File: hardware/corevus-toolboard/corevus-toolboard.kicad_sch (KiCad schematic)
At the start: 80 parts, among them J1 MF3, J10 1x3P, J2 XH, J3 MF3, J4 XH, J5 XH, J6 XH, J7 XH, J8 pinheader, J9 XH, Q2 NMOS, Q3 AO3401A, Q4 AO3400, Q5 AO3400, SW3 RST, U1 LIS2DE12, U2 TPS54302, U3 STM32G431KBU3, U4 TMC2209-LA, U5 MCP1416, U6 SPX3819M5-L-3-3, Y1 XRCGB25

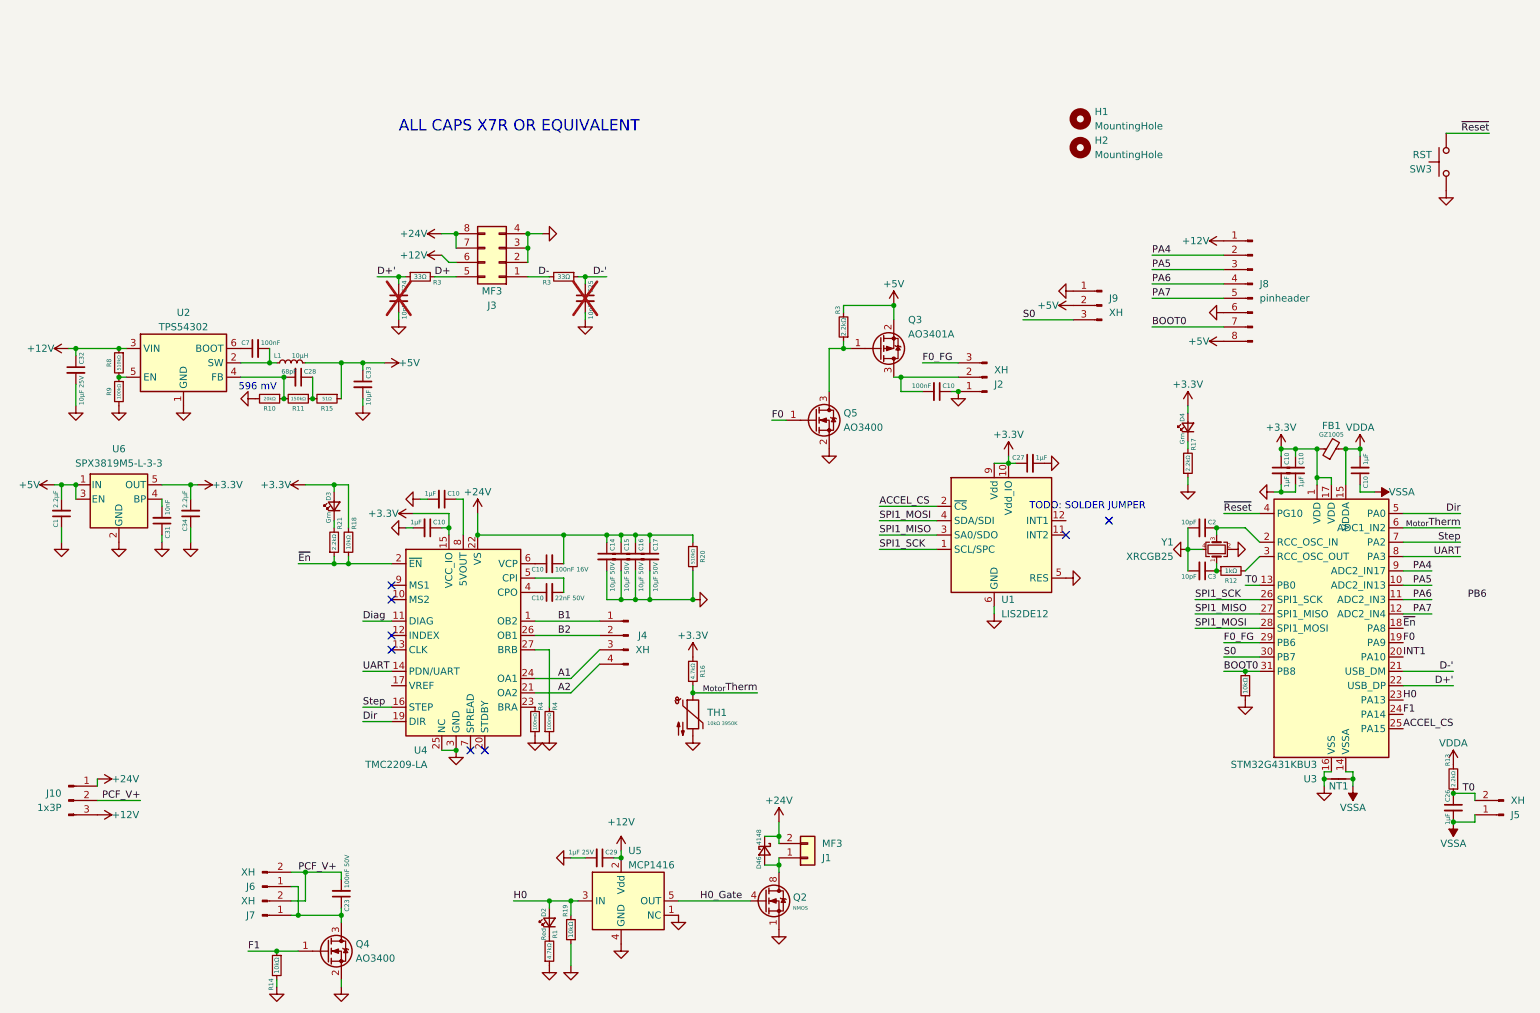
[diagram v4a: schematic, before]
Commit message: added ctb v0.3 and dual 2160, fixed typo in v0.6 manual
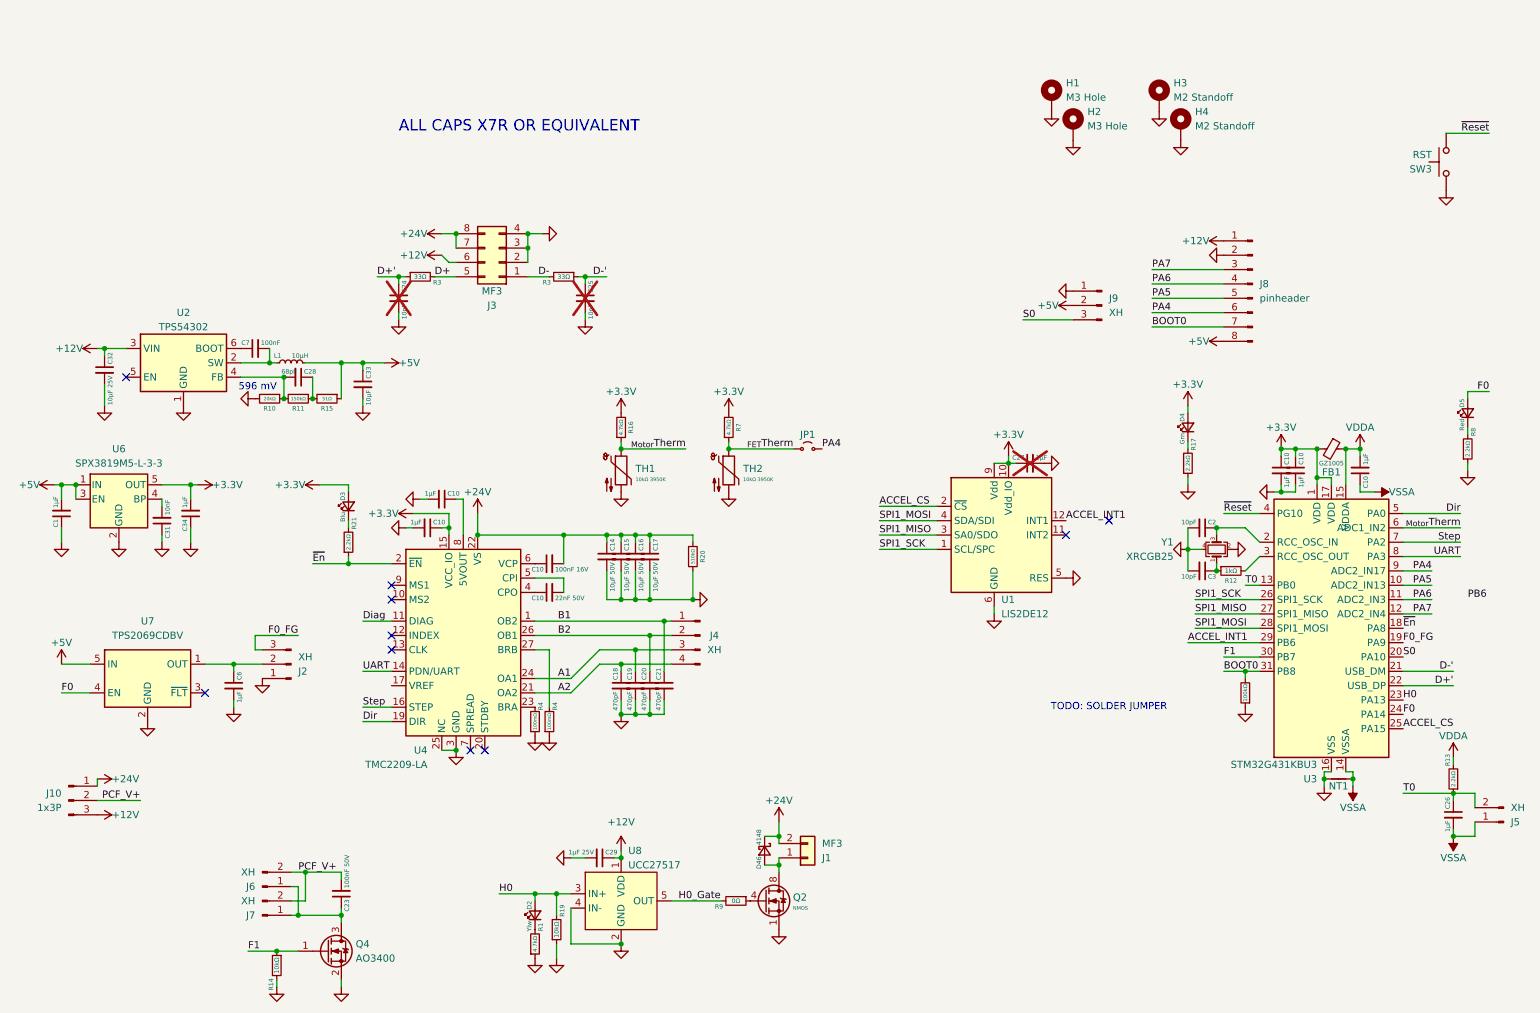
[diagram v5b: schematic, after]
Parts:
- removed C10: 100nF, AlphaLib:0402C, symbol Device:C_Small
- removed Q3: AO3401A, Package_TO_SOT_SMD:SOT-23, symbol Transistor_FET:AO3401A
- removed Q5: AO3400, Package_TO_SOT_SMD:SOT-23, symbol Device:Q_NMOS_GSD
- removed R18: 10kΩ, AlphaLib:0402R, symbol Device:R_Small
- removed R3: 2.2kΩ, AlphaLib:0402R, symbol Device:R_Small
- removed U5: MCP1416, Package_TO_SOT_SMD:SOT-23-5, symbol Driver_FET:MCP1416
- added C18, C19, C20, C21: 470pF, AlphaLib:0402C, symbol Device:C_Small
- added C6: 1µF, AlphaLib:0402C, symbol Device:C_Small
- added D5: Red, PCM_ME_passives:0603LED, symbol Device:LED_Small
- added H3, H4: M2 Standoff, corevus:Sinhoo_TH162010, symbol Mechanical:MountingHole_Pad
- added JP1: Jumper_2_Small_Open, Jumper:SolderJumper-2_P1.3mm_Open_RoundedPad1.0x1.5mm, symbol Jumper:Jumper_2_Small_Open
- added R7: 4.7kΩ, AlphaLib:0402R, symbol Device:R_Small
- added TH2: 10kΩ 3950K, AlphaLib:0402R, symbol Device:Thermistor_NTC
- added U7: TPS2069CDBV, Package_TO_SOT_SMD:SOT-23-5, symbol Power_Management:TPS2069CDBV
- added U8: UCC27517, Package_TO_SOT_SMD:SOT-23-5, symbol corevus:UCC27517
- C1, C34: value 2.2µF -> 1µF
- C27: now not fitted; now left out of the parts list
- D2: value Red -> Ylw; footprint corevus:XL1606 -> PCM_ME_passives:0603LED
- D3: value Grn -> Blu; footprint corevus:XL1606 -> PCM_ME_passives:0603LED
- D4: footprint AlphaLib:0402LED -> PCM_ME_passives:0603LED
- H1, H2: value MountingHole -> M3 Hole; footprint MountingHole:MountingHole_3.2mm_M3 -> corevus:MountingHole_M3_Driver_Corner; symbol Mechanical:MountingHole -> Mechanical:MountingHole_Pad; now left out of the parts list
- R3: value 10kΩ -> 100kΩ
- R8: value 510kΩ -> 2.2kΩ
- R9: value 100kΩ -> 0Ω
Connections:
- net INT1 is gone; now on net S0: U3.20 (PA10)
- net +12V: now also U8.1 (VDD); no longer R8.1
- net +3.3V: now also FB1.2, R7.2; no longer FB1.1
- net +5V: now also U7.5 (IN)
- net A1: now also C19.1
- net A2: now also C18.1
- net B1: now also C21.1
- net B2: now also C20.1
- net F0: now also U3.24 (PA14), D5.2 (A), U7.4 (EN); no longer U3.19 (PA9)
- net F0_FG: now also U3.19 (PA9); no longer U3.29 (PB6)
- net F1: now also U3.30 (PB7); no longer U3.24 (PA14)
- net GND: now also H1.1, H2.1, J8.2 (Pin_2), R8.1, C18.2, C19.2, C20.2, C21.2, C6.2, H3.1, H4.1, TH2.2, U7.2 (GND), U8.2 (GND), U8.4 (IN-); no longer J8.6 (Pin_6), R9.2
- net H0: now also U8.3 (IN+)
- net H0_Gate: now also R9.2, U8.5 (OUT); no longer Q2.4 (G)
- net PA4: now also J8.6 (Pin_6), JP1.2 (B); no longer J8.2 (Pin_2)
- net PA5: now also J8.5 (Pin_5); no longer J8.3 (Pin_3)
- net PA7: now also J8.3 (Pin_3); no longer J8.5 (Pin_5)
- net S0: no longer U3.30 (PB7)
- net VDDA: now also FB1.1; no longer FB1.2
- net ACCEL_INT1: now reaches U1.12 (INT1)
- net ACCEL_INT1: now also U3.29 (PB6)
- net at J2.2 (Pin_2): now also C6.1, U7.1 (OUT)
- new net: Q2.4 (G), R9.1
- new net: D5.1 (K), R8.2
- new net _{FET}Therm: JP1.1 (A), R7.1, TH2.1
- now unconnected: U2.5 (EN)
- no-connect marks 8 -> 10
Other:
- moved on the sheet: C26, C32, D2, D3, FB1, J2, J4, J5, R1, R16, R19, R21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

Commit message: last before i go on v0.7
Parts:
- C29: value 1µF 25V -> 100nF 25V
- C7: LCSC C1525 -> (none)
- D2: value Ylw -> Red
- D3: value Blu -> Grn
- D4: value Grn -> Wht
- D5: value Red -> Ylw
- H3, H4: now in the parts list
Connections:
- net +3.3V: now also J8.8 (Pin_8), R17.2; no longer D4.2 (A)
- net +5V: no longer J8.8 (Pin_8)
- net F0: now also R8.2; no longer D5.2 (A)
- net GND: now also D2.1 (K), D4.1 (K), D5.1 (K); no longer R1.1, R17.1, R8.1
- net H0: now also R1.2; no longer D2.2 (A)
- new net: D4.2 (A), R17.1
- new net: D5.2 (A), R8.1
- new net: D2.2 (A), R1.1
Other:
- moved on the sheet: D2, D4, D5, R1, R17, R8

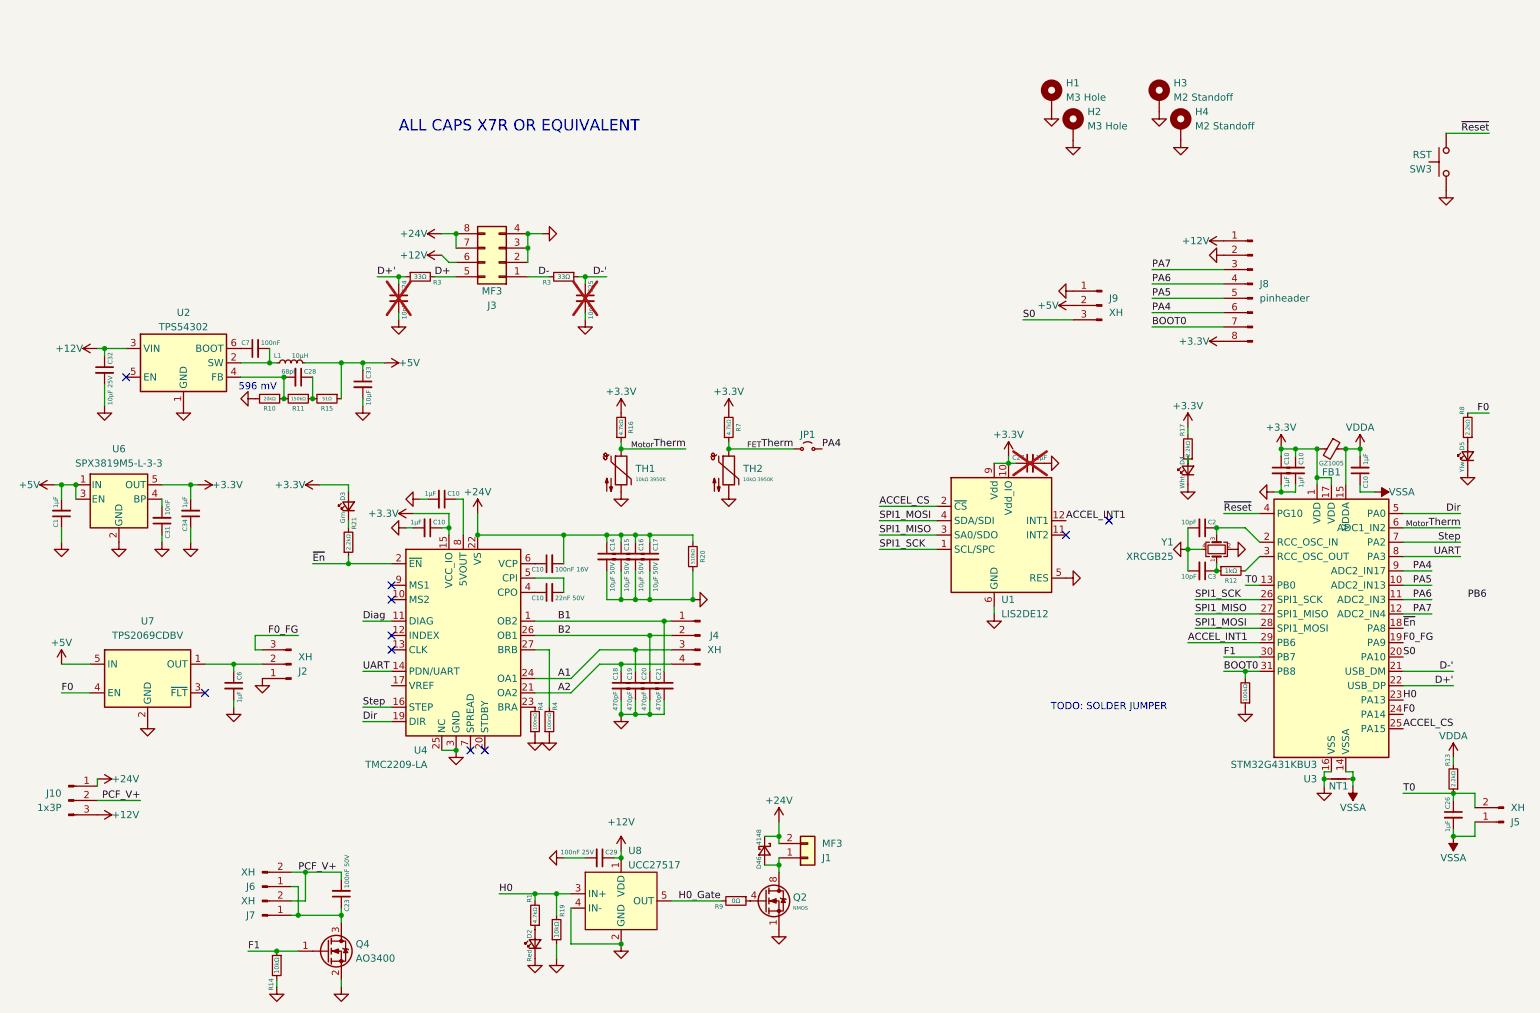
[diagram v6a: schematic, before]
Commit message: cleaned up corevus toolboard schematics to be more presentable
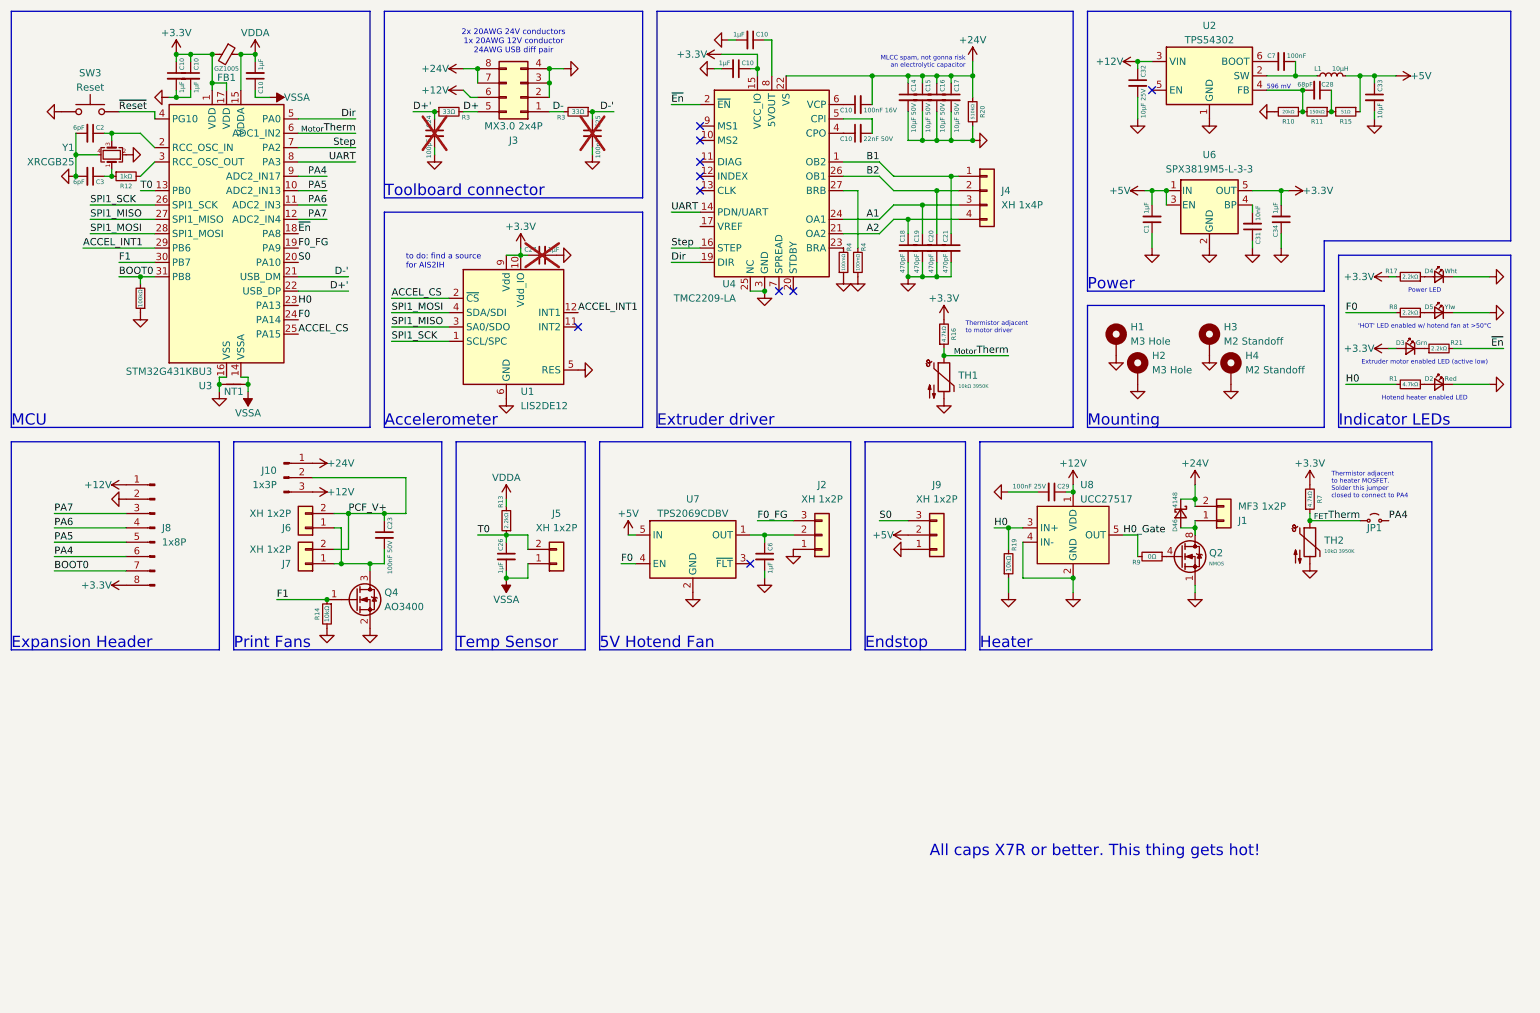
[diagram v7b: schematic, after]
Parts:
- C2, C3: value 10pF -> 6pF
- C23: value 100nF 50V -> 100nF 50V
- C24, C25: value 10pF -> 100pF
- C28: value 68pF -> 68pF
- C7: value 100nF -> 100nF
- J1: value MF3 -> MF3 1x2P
- J2, J9: value XH -> XH 1x2P; symbol Connector:Conn_01x03_Pin -> Connector_Generic:Conn_01x03
- J3: value MF3 -> MX3.0 2x4P
- J4: value XH -> XH 1x4P; symbol Connector:Conn_01x04_Pin -> Connector_Generic:Conn_01x04
- J5, J6, J7: value XH -> XH 1x2P; symbol Connector:Conn_01x02_Pin -> Connector_Generic:Conn_01x02
- J8: value pinheader -> 1x8P
- SW3: value RST -> Reset
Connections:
- net PCF_V+: now also C23.1; no longer C23.2
- net ~{En}: now also R21.2; no longer R21.1
- net at J6.1 (Pin_1), J7.1 (Pin_1), Q4.3 (D): now also C23.2; no longer C23.1
- net at D3.1 (K): now also R21.1; no longer R21.2
- net Diag: no longer names the net of U4.11 (DIAG)
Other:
- note added: "'HOT' LED enabled w/ hotend fan at >50°C"
- note added: "2x 20AWG 24V conductors 1x 20AWG 12V conductor 24AWG USB diff pair"
- note added: "5V Hotend Fan"
- note added: "Accelerometer"
- note added: "All caps X7R or better. This thing gets hot!"
- note added: "Endstop"
- note added: "Expansion Header"
- note added: "Extruder driver"
- note added: "Extruder motor enabled LED (active low)"
- note added: "Heater"
- note added: "Hotend heater enabled LED"
- note added: "Indicator LEDs"
- note added: "MCU"
- note added: "MLCC spam, not gonna risk an electrolytic capacitor"
- note added: "Mounting"
- note added: "Power"
- note added: "Power LED"
- note added: "Print Fans"
- note added: "Temp Sensor"
- note added: "Thermistor adjacent to heater MOSFET. Solder this jumper closed to connect to PA4"
- note added: "Thermistor adjacent to motor driver"
- note added: "Toolboard connector"
- note added: "to do: find a source for AIS2IH"
- note removed: "ALL CAPS X7R OR EQUIVALENT"
- note removed: "TODO: SOLDER JUMPER"
- company: (none) -> Meridi Engineering
- title: (none) -> Corevus Toolboard
- moved on the sheet: C1, C10, C14, C15, C16, C17, C18, C19, C2, C20, C21, C23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
